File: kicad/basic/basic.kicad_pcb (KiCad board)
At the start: 2 copper layers, 50 x 50 mm, 21 parts, among them P2 CONN_01X15, P3 CONN_01X15, P4 CONN_01X06, P5 CONN_01X01, P6 CONN_01X01, P7 CONN_01X01, P8 CONN_01X01, P9 CONN_01X06, SW1 SW_PUSH, SW2 SW_PUSH

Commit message: Gerbers
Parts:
- added G***: LOGO, denbit:LOGO, B.Cu at (145.3, 108.2)
- moved G*** 0.25 mm to (145.8, 113.3)
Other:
- board text added: "NodeMCU v1.0 goes here"

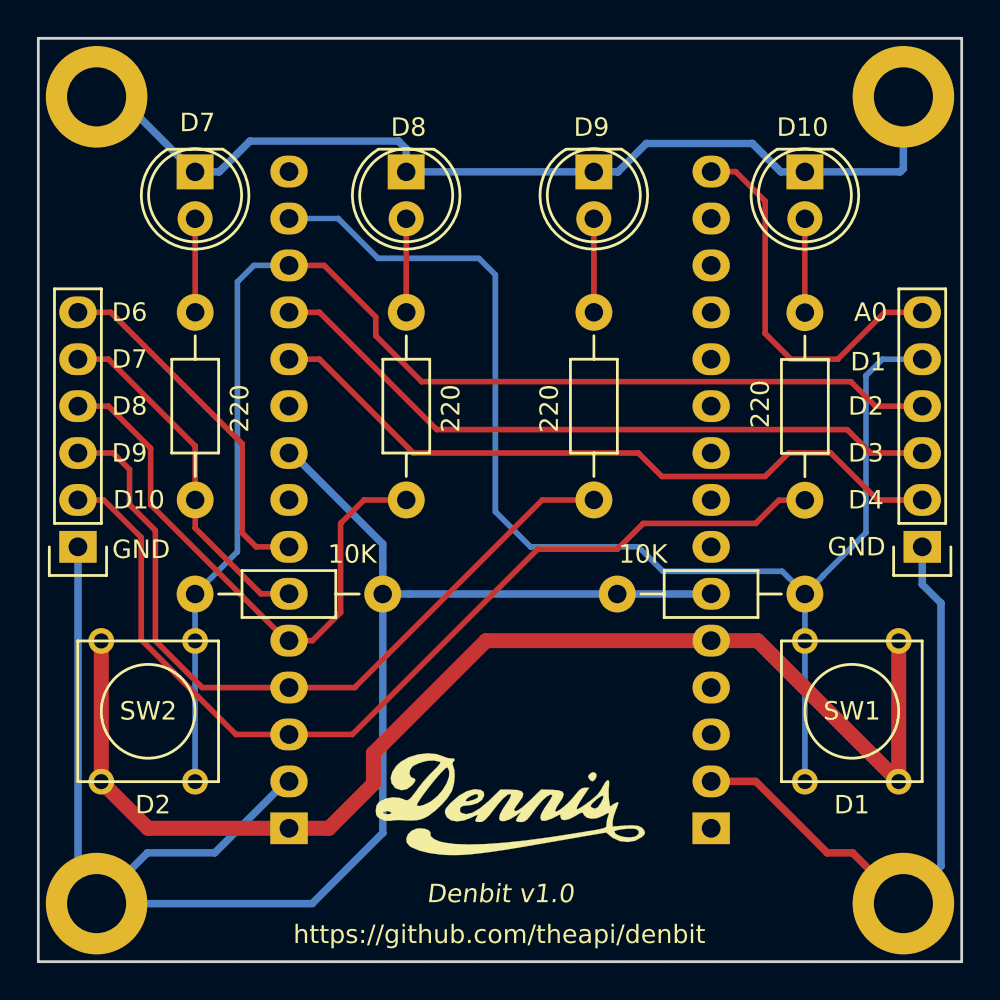
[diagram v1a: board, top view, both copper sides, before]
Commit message: RGB led
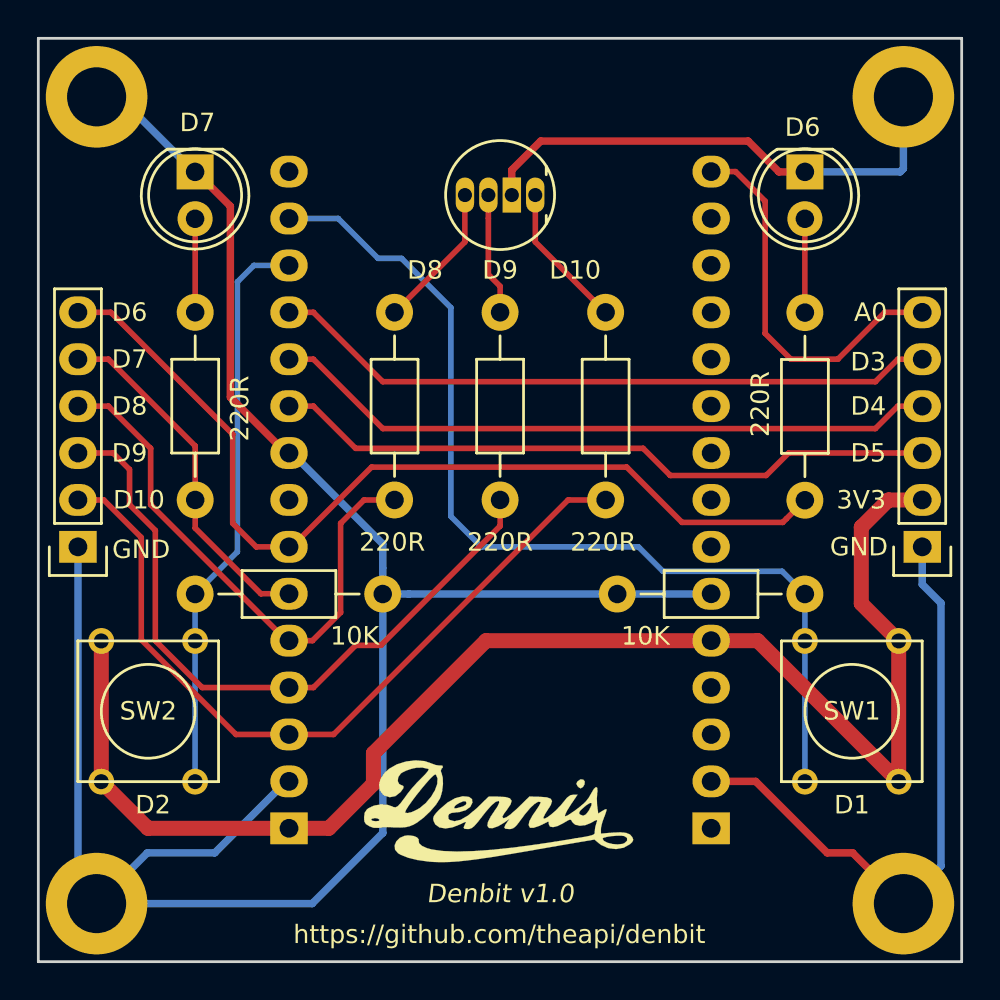
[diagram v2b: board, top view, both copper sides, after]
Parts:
- removed D3: LED, LEDs:LED-5MM
- added R7: 220R, Resistors_ThroughHole:Resistor_Horizontal_RM10mm, F.Cu at (151.0, 86.7)
- D2: value LED -> LED_RCBG; footprint LEDs:LED-5MM -> LEDs:LED-RGB-5MM_Common_Cathode
- R3, R4, R5, R6: value 220 -> 220R
- moved R6 10.8 mm to (139.6, 86.7)
- moved D2 7.10 mm to (147.2, 80.3)
- moved R5 5.08 mm to (145.3, 86.7)
- moved G*** 0.74 mm to (145.2, 113.7)
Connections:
- D2 pad 1: GND -> Net-(D2-Pad1)
- D2 pad 2: Net-(D2-Pad2) -> GND
- P3 pad 10: Net-(P3-Pad10) -> D5
- P4 pad 2: D4 -> 3V3
- P4 pad 3: D3 -> D5
- P4 pad 4: D2 -> D4
- P4 pad 5: D1 -> D3
- R4 pad 2: D10 -> D6
- R5 pad 1: Net-(D2-Pad2) -> Net-(D2-Pad3)
- R5 pad 2: D8 -> D9
- R6 pad 1: Net-(D3-Pad2) -> Net-(D2-Pad4)
- R6 pad 2: D9 -> D8
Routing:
- net D2: track 69.2 -> 31.2 mm
- net D5: track 0.00 -> 36.3 mm
- net D6: track 19.5 -> 51.0 mm
- net D1: track 70.8 -> 53.3 mm
- net 3V3: track 68.0 -> 78.9 mm
- net D10: track 53.1 -> 42.3 mm
- net Net-(D2-Pad4): track 0.00 -> 7.93 mm
- net Net-(D2-Pad1): track 0.00 -> 7.93 mm
- net Net-(D2-Pad3): track 0.00 -> 6.61 mm
- net Net-(D3-Pad2): track 5.07 -> 0.00 mm
- net Net-(D2-Pad2): track 5.07 -> 0.00 mm
- net D9: track 42.0 -> 37.8 mm
- net D4: track 38.5 -> 36.3 mm
- net D3: track 37.4 -> 36.3 mm
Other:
- board text added: "3V3"
- board text added: "D5"
- board text added: "NodeMCU goes here"
- board text removed: "NodeMCU v1.0 goes here"

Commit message: Layout tweaks
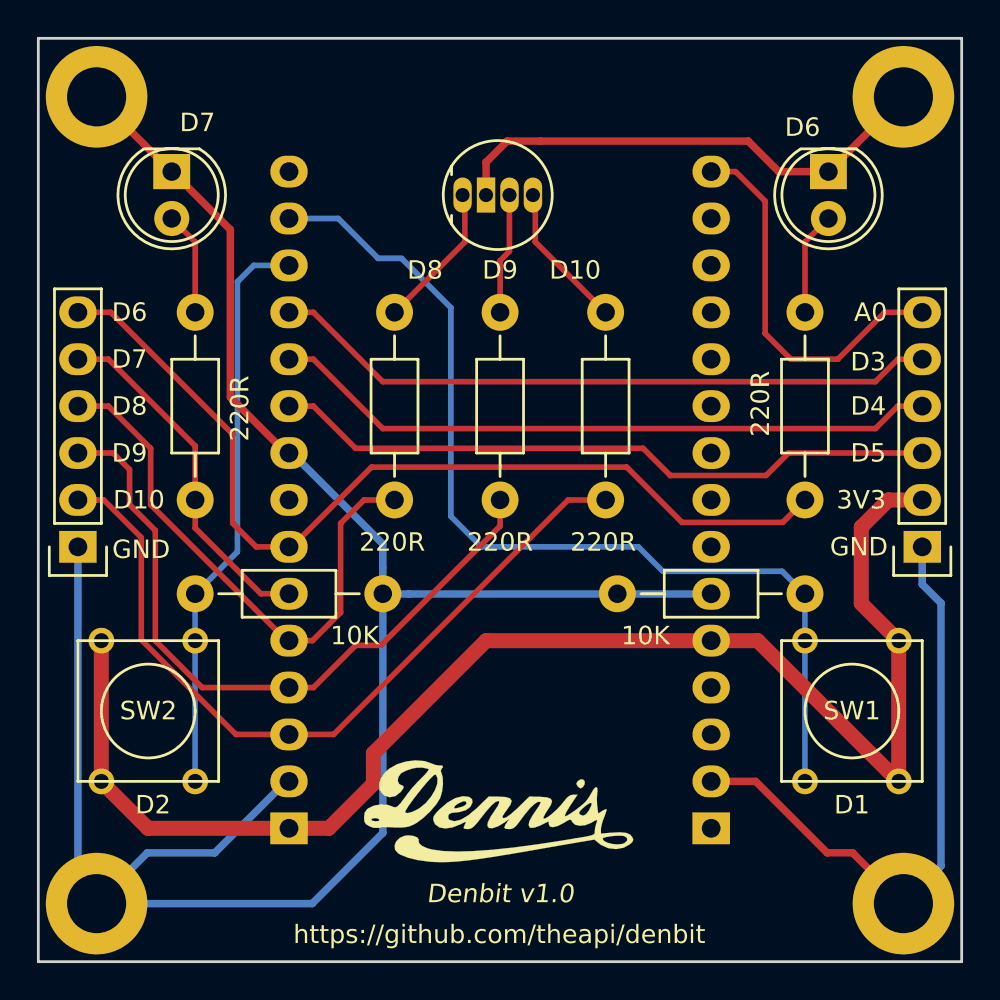
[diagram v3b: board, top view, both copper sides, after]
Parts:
- moved D2 3.94 mm to (143.3, 80.3), turned to 90 degrees
- moved D4 1.28 mm to (163.1, 79.0)
- moved D1 1.27 mm to (127.6, 79.0)
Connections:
- R6 pad 1: Net-(D2-Pad4) -> Net-(D2-Pad1)
- R7 pad 1: Net-(D2-Pad1) -> Net-(D2-Pad4)
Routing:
- net GND: track 176.6 -> 175.2 mm
- net Net-(D1-Pad2): track 5.07 -> 5.61 mm
- net Net-(D4-Pad2): track 5.08 -> 5.61 mm

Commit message: Resistor values
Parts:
- R3, R4, R6: value 220R -> 150R
- R5, R7: value 220R -> 100R
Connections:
- net Net-(D1-Pad2) renamed /S_GREEN
- net Net-(D2-Pad1) renamed /RGB_RED
- net Net-(D2-Pad3) renamed /RGB_GREEN
- net Net-(D2-Pad4) renamed /RGB_BLUE
- net Net-(D4-Pad2) renamed /S_RED

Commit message: Changed pin assignments
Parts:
- moved G*** 1.52 mm to (145.3, 106.7)
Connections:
- P2 pad 12: Net-(P2-Pad12) -> SD3
- P3 pad 15: Net-(P3-Pad15) -> D0
- P3 pad 3: D10 -> Net-(P3-Pad3)
- P3 pad 4: D9 -> Net-(P3-Pad4)
- P4 pad 3: D5 -> D4
- P4 pad 4: D4 -> D3
- P4 pad 5: D3 -> D0
- P9 pad 2: D10 -> 3V3
- P9 pad 3: D9 -> D8
- P9 pad 4: D8 -> D7
- P9 pad 5: D7 -> D6
- P9 pad 6: D6 -> D5
- R5 pad 2: D9 -> SD3
- R7 pad 2: D10 -> D5
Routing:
- net D0: track 0.00 -> 44.8 mm
- net D10: track 42.3 -> 0.00 mm
- net D9: track 37.8 -> 0.00 mm
- net GND: track 175.2 -> 157.4 mm
- net SD3: track 0.00 -> 15.8 mm
- net 3V3: track 78.9 -> 89.6 mm
- net D5: track 36.3 -> 32.8 mm
- net D7: track 19.3 -> 17.6 mm
- net D8: track 30.8 -> 29.2 mm
- net D6: track 51.0 -> 49.7 mm
- net D1: track 53.3 -> 54.3 mm
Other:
- board text added: "0"
- board text added: "10"
- board text added: "12"
- board text added: "13"
- board text added: "14"
- board text added: "15"
- board text added: "16"
- board text added: "2"
- board text added: "RGB"
- board text added: "peter_clarke@dennis.co.uk"
- board text removed: "D10"
- board text removed: "D3"
- board text removed: "D4"
- board text removed: "D5"
- board text removed: "D6"
- board text removed: "D7"
- board text removed: "D8"
- board text removed: "D9"

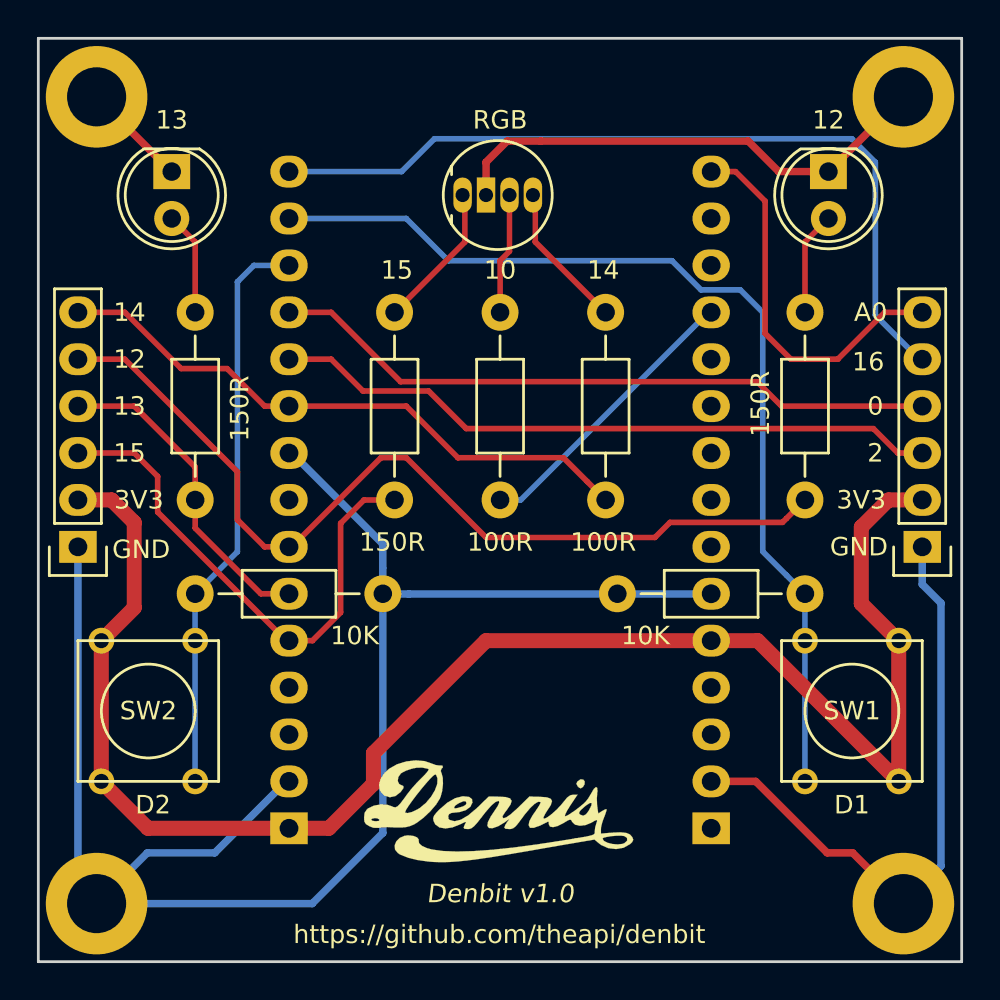
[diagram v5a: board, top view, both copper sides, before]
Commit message: I2C & SPI on the headers
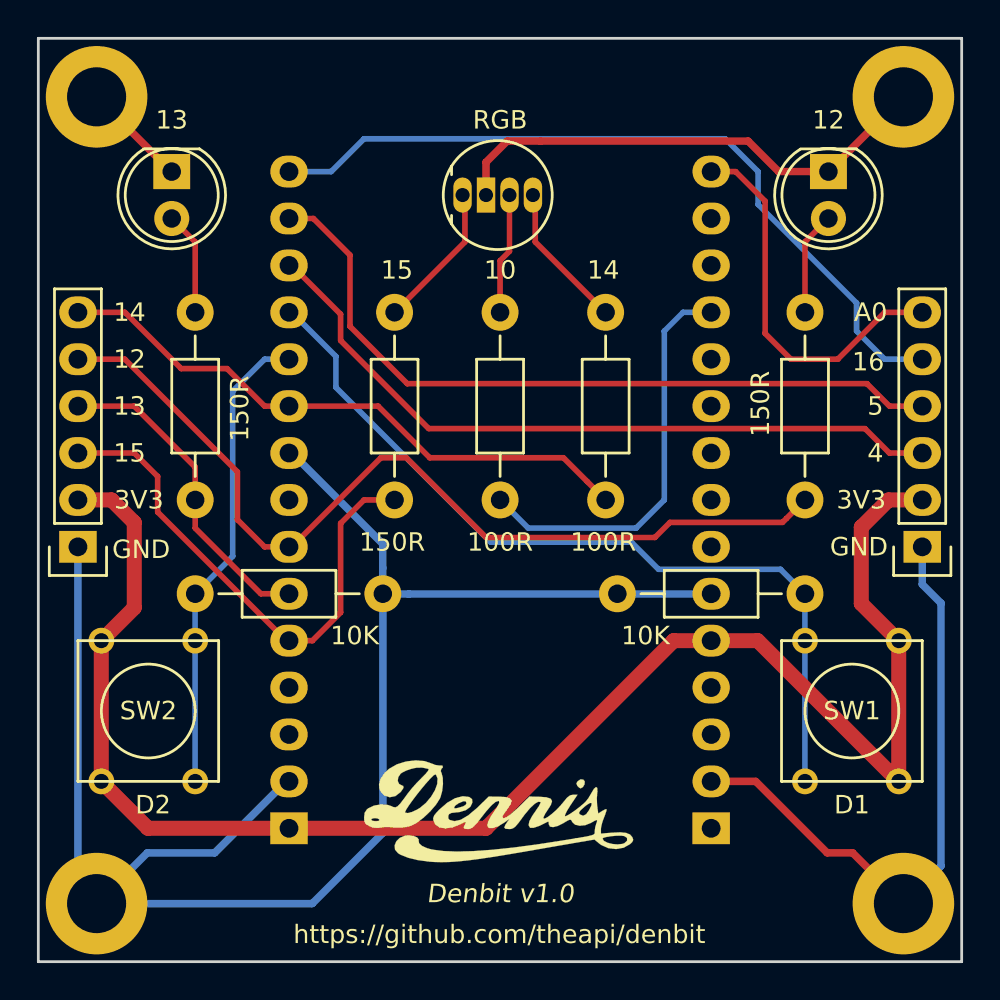
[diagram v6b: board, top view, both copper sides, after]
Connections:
- net A0 renamed ADC0
- net D0 renamed GPIO16
- net D5 renamed GPIO14
- net D6 renamed GPIO12
- net D7 renamed GPIO13
- net D8 renamed GPIO15
- net SD3 renamed GPIO10
- P3 pad 11: D4 -> GPIO2
- P3 pad 12: D3 -> GPIO0
- P3 pad 13: D2 -> GPIO4
- P3 pad 14: D1 -> GPIO5
- P4 pad 3: D4 -> GPIO4
- P4 pad 4: D3 -> GPIO5
- R1 pad 2: D1 -> GPIO0
- R2 pad 2: D2 -> GPIO2
- SW1 pad 2: D1 -> GPIO0
- SW2 pad 2: D2 -> GPIO2
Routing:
- net D1: track 54.3 -> 0.00 mm
- net GPIO0: track 0.00 -> 45.4 mm
- net GPIO5: track 0.00 -> 40.9 mm
- net GPIO4: track 0.00 -> 39.3 mm
- net D3: track 36.4 -> 0.00 mm
- net D4: track 36.4 -> 0.00 mm
- net D2: track 31.2 -> 0.00 mm
- net GPIO2: track 0.00 -> 25.7 mm
- net GPIO10: track 15.8 -> 22.6 mm
- net GPIO16: track 44.8 -> 41.9 mm
- net 3V3: track 89.6 -> 88.6 mm
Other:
- board text added: "4"
- board text added: "5"
- board text removed: "0"
- board text removed: "2"

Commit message: Pin tweaks
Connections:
- P3 pad 10: GPIO14 -> Net-(P3-Pad10)
- P3 pad 8: Net-(P3-Pad8) -> GPIO14
- R5 pad 2: GPIO10 -> GPIO14
- R7 pad 2: GPIO14 -> GPIO10
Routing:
- net GPIO10: track 22.6 -> 14.7 mm
- net GPIO14: track 32.8 -> 31.0 mm
- net GPIO4: track 39.3 -> 40.4 mm
- net GPIO0: track 45.4 -> 46.2 mm

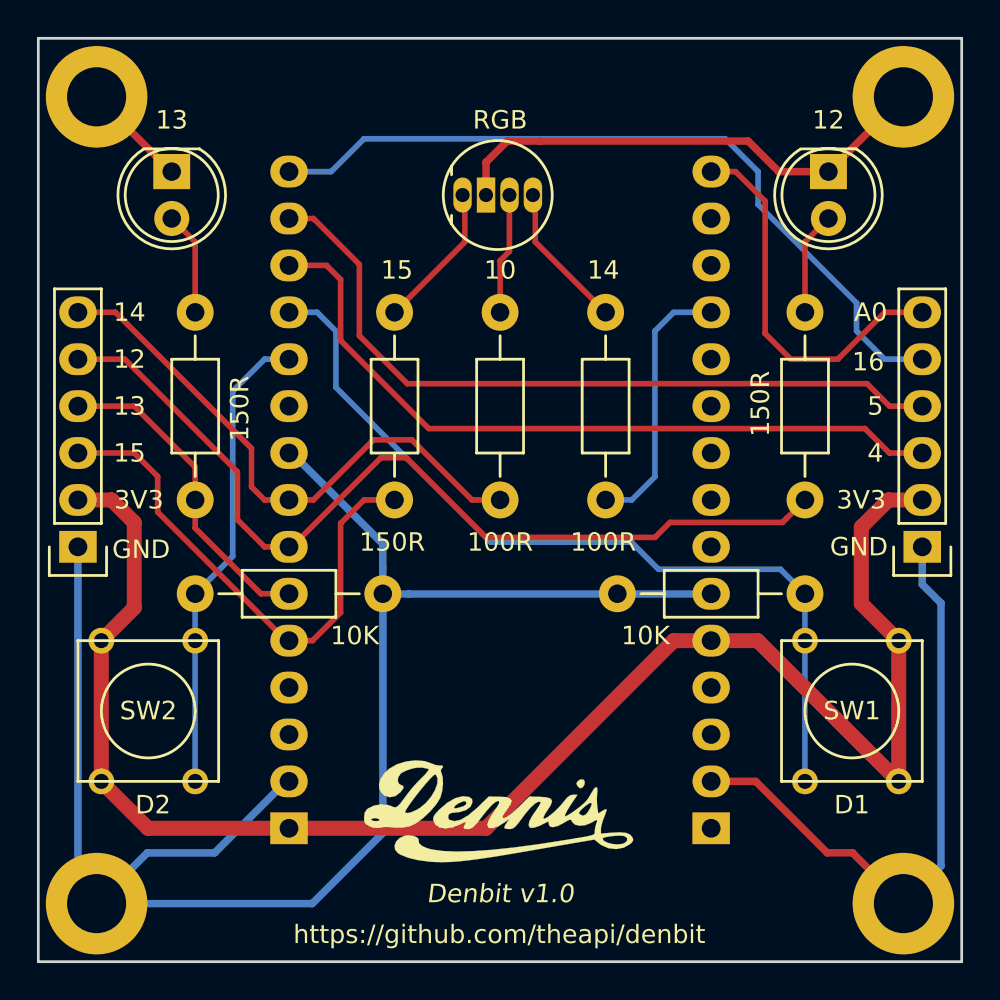
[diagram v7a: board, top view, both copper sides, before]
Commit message: Internal pullup on the switches
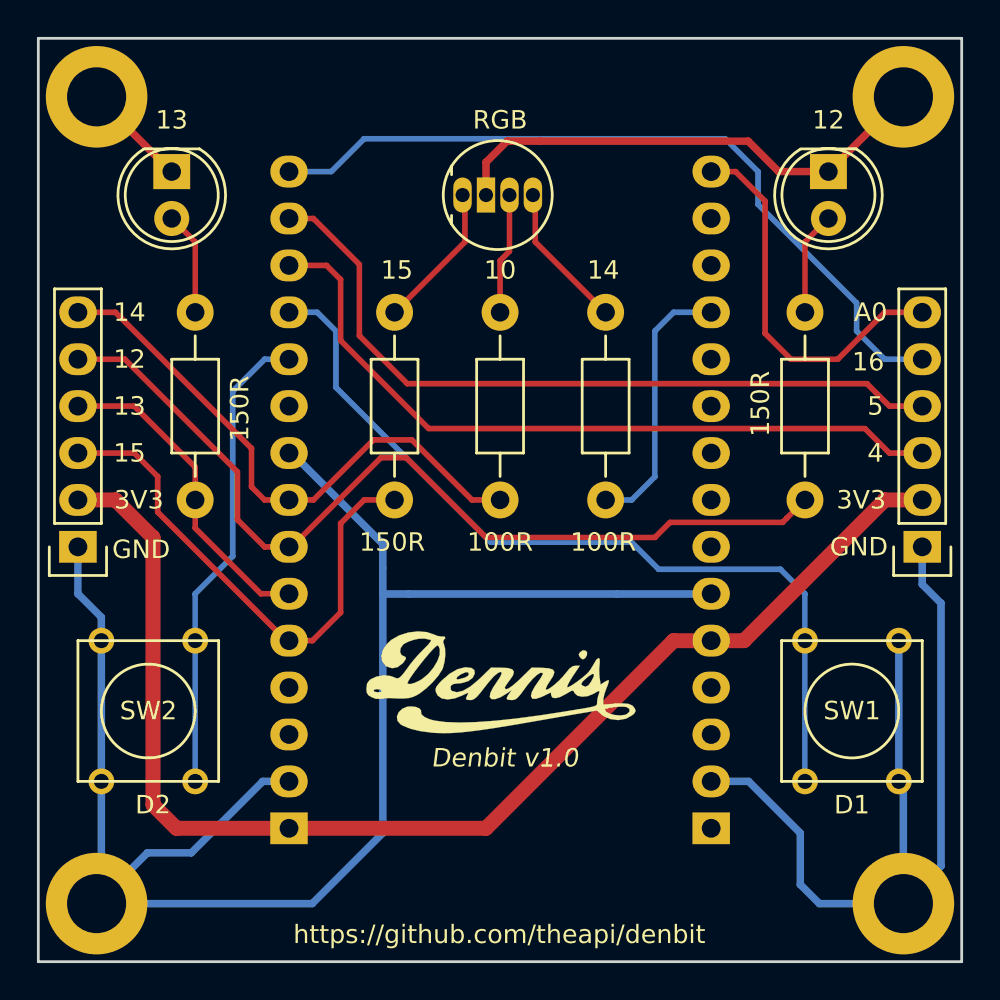
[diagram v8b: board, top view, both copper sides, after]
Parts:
- removed R1, R2: 10K, Resistors_ThroughHole:Resistor_Horizontal_RM10mm
- moved G*** 6.99 mm to (145.3, 106.7)
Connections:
- SW1 pad 1: 3V3 -> GND
- SW2 pad 1: 3V3 -> GND
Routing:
- net 3V3: track 88.6 -> 69.1 mm
- net GND: track 157.4 -> 175.2 mm
